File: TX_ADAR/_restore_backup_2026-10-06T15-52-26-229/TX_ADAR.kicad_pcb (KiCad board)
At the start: 4 copper layers, 68 x 156.9 mm, 58 parts, among them IC1 REG1117A-1.8, IC2 REG1117A-2.5, J1 Screw_Terminal_01x02, J10 Conn_Coaxial, J11 RJ45_LED_Shielded, J12 RJ45_LED_Shielded, J16 RJ45_LED_Shielded, J2 Conn_Coaxial, J21 Conn_01x04, J3 Conn_Coaxial, J4 Conn_Coaxial, J5 Conn_Coaxial, J6 Conn_Coaxial, J7 Conn_Coaxial, J8 Conn_Coaxial, J9 Conn_Coaxial, SW1 SW_SPDT, SW2 SW_SPDT, SW3 SW_SPDT, SW9 SW_SPDT, U10 TXB0101DBV, U11 TXB0101DBV, U14 TXB0101DBV, U19 TXB0101DBV, U2 ADAR2001ACCZ

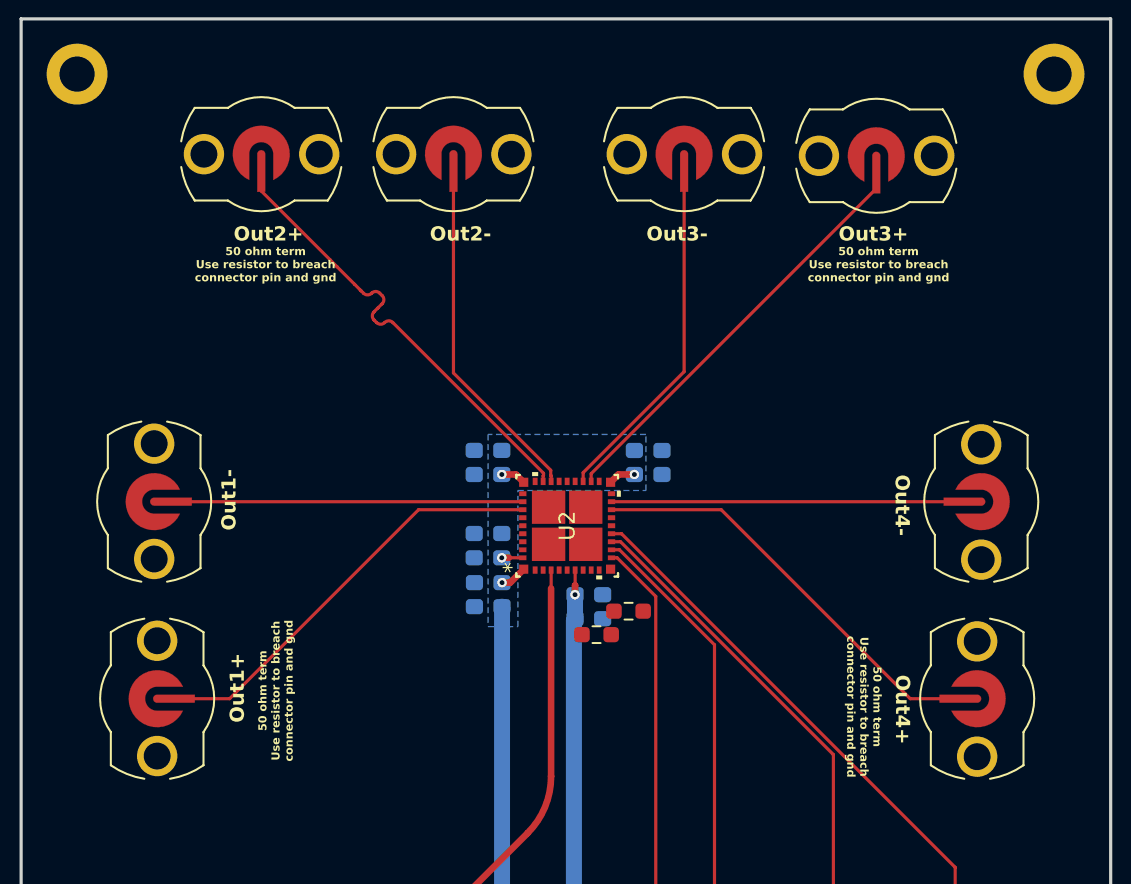
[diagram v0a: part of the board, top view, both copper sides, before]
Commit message: Updated routing
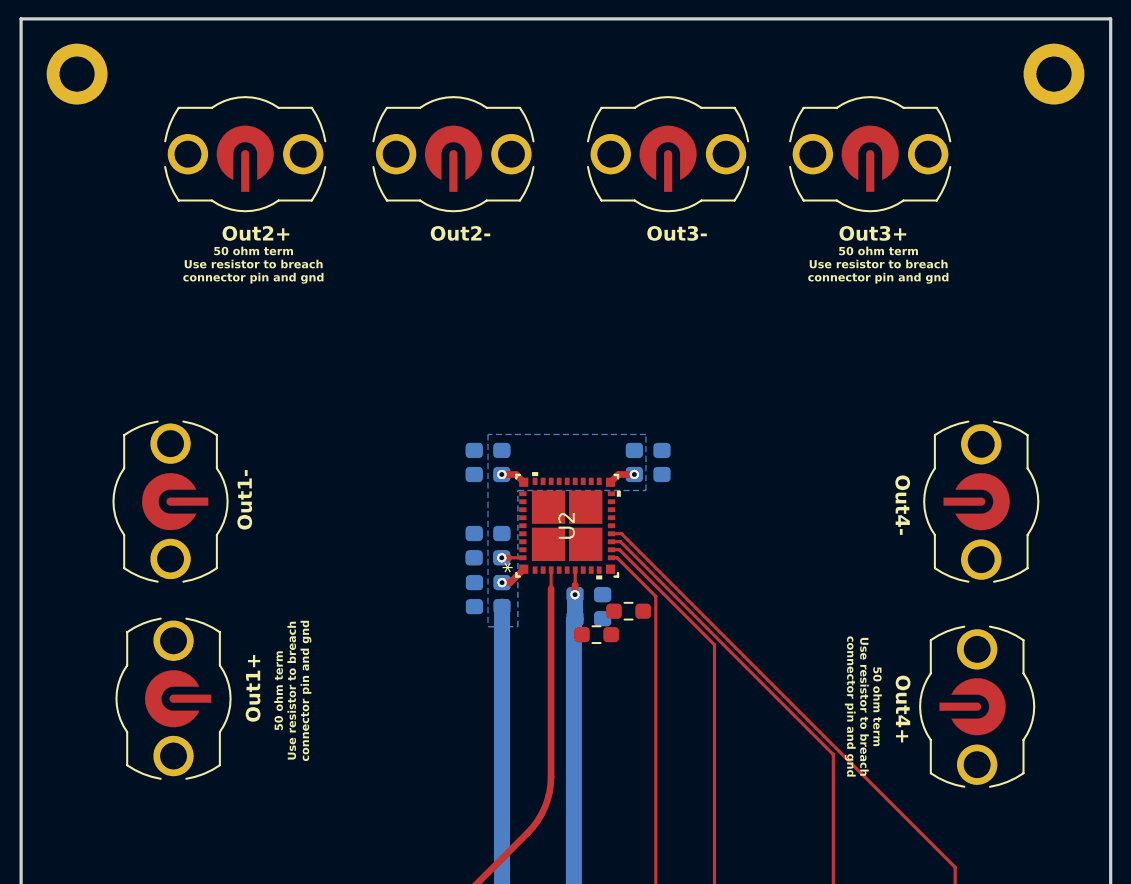
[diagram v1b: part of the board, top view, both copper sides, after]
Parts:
- moved J3 1.02 mm to (97.5, 71.0)
- moved J4 1.02 mm to (97.3, 58.7)
- moved J5 1.00 mm to (102.0, 37.0)
- moved J8 1.00 mm to (128.4, 37.0)
- moved J9 0.50 mm to (147.7, 71.5)
- moved J7 0.39 mm to (141.0, 37.0)
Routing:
- net /RFOut1+: track 27.7 -> 0.00 mm
- net /RFOut4+: track 27.8 -> 0.04 mm
- net /RFOut3+: track 27.7 -> 0.00 mm
- net /RFOut2+: track 27.7 -> 0.00 mm
- net /RFOut4-: track 23.2 -> 0.08 mm
- net /RFOut3-: track 23.0 -> 0.00 mm
- net /RFOut1-: track 23.0 -> 0.01 mm
- net /RFOut2-: track 23.0 -> 0.00 mm
